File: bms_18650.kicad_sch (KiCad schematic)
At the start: 8 parts, among them IC1 BQ298000RUGR, IC2 EFC8811R-TF

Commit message: updates
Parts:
- added J1: ~, Library:ENFITNIX_BAT, symbol enfitnix_bat_connector:concentric_rings
- C1, C2: footprint (none) -> Capacitor_SMD:C_0805_2012Metric_Pad1.18x1.45mm_HandSolder
- R3, R4, R5: footprint (none) -> Resistor_SMD:R_0805_2012Metric_Pad1.20x1.40mm_HandSolder
- R_SEN1: renamed from R_SEN; footprint (none) -> Resistor_SMD:R_0805_2012Metric_Pad1.20x1.40mm_HandSolder
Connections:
- net GND: now also J1.2 (-)
- net LINK+: now also J1.1 (+)
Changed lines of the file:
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@@
+	)
+	(junction
+		(at 151.13 54.61)
+		(diameter 0)
+		(color 0 0 0 0)
 	)
 	(junction
@@
 	)
 	(junction
+		(at 151.13 124.46)
+		(diameter 0)
+		(color 0 0 0 0)
+	)
+	(junction
 		(at 107.95 124.46)
 		(diameter 0)
@@
 	(wire
 		(pts
-			(xy 140.97 54.61) (xy 157.48 54.61)
+			(xy 140.97 54.61) (xy 151.13 54.61)
 		)
 		(stroke
@@
 	(wire
 		(pts
+			(xy 151.13 67.31) (xy 151.13 54.61)
+		)
+		(stroke
+			(width 0)
+			(type default)
+		)
+	)
+	(wire
+		(pts
 			(xy 55.88 54.61) (xy 55.88 71.12)
 		)
@@
 	(wire
 		(pts
+			(xy 151.13 54.61) (xy 157.48 54.61)
+		)
+		(stroke
+			(width 0)
+			(type default)
+		)
+	)
+	(wire
+		(pts
 			(xy 121.92 54.61) (xy 133.35 54.61)
 		)
@@
 	(wire
 		(pts
-			(xy 107.95 124.46) (xy 153.67 124.46)
+			(xy 107.95 124.46) (xy 151.13 124.46)
+		)
+		(stroke
+			(width 0)
+			(type default)
+		)
+	)
+	(wire
+		(pts
+			(xy 151.13 124.46) (xy 153.67 124.46)
 		)
 		(stroke
@@
 	(wire
 		(pts
+			(xy 151.13 73.66) (xy 151.13 124.46)
+		)
+		(stroke
+			(width 0)
+			(type default)
+		)
+	)
+	(wire
+		(pts
 			(xy 140.97 97.79) (xy 140.97 54.61)
 		)
@@
 	(wire
 		(pts
+			(xy 158.75 67.31) (xy 151.13 67.31)
+		)
+		(stroke
+			(width 0)
+			(type default)
+		)
+	)
+	(wire
+		(pts
 			(xy 55.88 71.12) (xy 55.88 97.79)
 		)
@@
 		(pts
 			(xy 107.95 124.46) (xy 92.71 124.46)
+		)
+		(stroke
+			(width 0)
+			(type default)
+		)
+	)
+	(wire
+		(pts
+			(xy 158.75 73.66) (xy 151.13 73.66)
 		)
 		(stroke
@@
 			)
 		)
-		(property "Footprint" ""
+		(property "Footprint" "Capacitor_SMD:C_0805_2012Metric_Pad1.18x1.45mm_HandSolder"
 			(at 78.4352 97.79 0)
 			(effects
@@
 			)
 		)
-		(property "Footprint" ""
+		(property "Footprint" "Capacitor_SMD:C_0805_2012Metric_Pad1.18x1.45mm_HandSolder"
 			(at 78.4352 78.74 0)
 			(effects
@@
 				(path "/463bbe92-7f47-47ca-96a4-4d541ad2c704"
 					(reference "C1")
+					(unit 1)
+				)
+			)
+		)
+	)
+	(symbol
+		(lib_id "enfitnix_bat_connector:concentric_rings")
+		(at 168.91 67.31 0)
+		(unit 1)
+		(exclude_from_sim no)
+		(in_bom yes)
+		(on_board yes)
+		(dnp no)
+		(fields_autoplaced yes)
+		(property "Reference" "J1"
+			(at 177.8 66.6749 0)
+			(effects
+				(font
+					(size 1.27 1.27)
+				)
+				(justify left)
+			)
+		)
+		(property "Value" "~"
+			(at 177.8 68.58 0)
+			(effects
+				(font
+					(size 1.27 1.27)
+				)
+				(justify left)
+			)
+		)
+		(property "Footprint" "Library:ENFITNIX_BAT"
+			(at 168.91 67.31 0)
+			(effects
+				(font
+					(size 1.27 1.27)
+				)
+				(hide yes)
+			)
+		)
+		(property "Datasheet" ""
+			(at 168.91 67.31 0)
+			(effects
+				(font
+					(size 1.27 1.27)
+				)
+				(hide yes)
+			)
+		)
+		(property "Description" ""
+			(at 168.91 67.31 0)
+			(effects
+				(font
+					(size 1.27 1.27)
+				)
+				(hide yes)
+			)
+		)
+		(pin "1"
+		)
+		(pin "2"
+		)
+		(instances
+			(project ""
+				(path "/463bbe92-7f47-47ca-96a4-4d541ad2c704"
+					(reference "J1")
 					(unit 1)
 				)
@@
 			)
 		)
-		(property "Footprint" ""
+		(property "Footprint" "Resistor_SMD:R_0805_2012Metric_Pad1.20x1.40mm_HandSolder"
 			(at 137.16 96.012 90)
 			(effects
@@
 		(dnp no)
 		(fields_autoplaced yes)
-		(property "Reference" "R_SEN"
+		(property "Reference" "R_SEN1"
 			(at 110.49 116.8399 0)
 			(effects
@@
 			)
 		)
-		(property "Footprint" ""
+		(property "Footprint" "Resistor_SMD:R_0805_2012Metric_Pad1.20x1.40mm_HandSolder"
 			(at 106.172 118.11 90)
 			(effects
@@
 			(project ""
 				(path "/463bbe92-7f47-47ca-96a4-4d541ad2c704"
-					(reference "R_SEN")
+					(reference "R_SEN1")
 					(unit 1)
 				)
@@
 			)
 		)
-		(property "Footprint" ""
+		(property "Footprint" "Resistor_SMD:R_0805_2012Metric_Pad1.20x1.40mm_HandSolder"
 			(at 67.31 96.012 90)
 			(effects
@@
 			)
 		)
-		(property "Footprint" ""
+		(property "Footprint" "Resistor_SMD:R_0805_2012Metric_Pad1.20x1.40mm_HandSolder"
 			(at 67.31 69.342 90)
 			(effects

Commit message: first ordered revision
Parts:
- added J2: ~, Library:CELL_LEAD_CONN, symbol enfitnix_bat_connector:two_conn_leads
- C1, C2: value 0.1uF -> 100n
- IC1: value BQ298000RUGR -> BQ298218RUGR; LCSC (none) -> C36857140
- IC2: LCSC (none) -> C895369
- J1: now not fitted
- R3: value 330 -> 330R
- R4: value 20 -> 20R
- R5: value 2k -> 2K
- R_SEN1: value 0.001 -> 0R001; LCSC (none) -> C4337252
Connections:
- net CELL+: now also J2.1 (CELL+)
- net GND: now also J2.2 (CELL-)
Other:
- note added: "BQ298218 has OCC=-18mV and OCD=40mV so max current with R_SEN1=1mOhm => dchg: 40A => chg: 18A"
- moved on the sheet: C1, C2, IC1, IC2, R3, R4, R5, R_SEN1

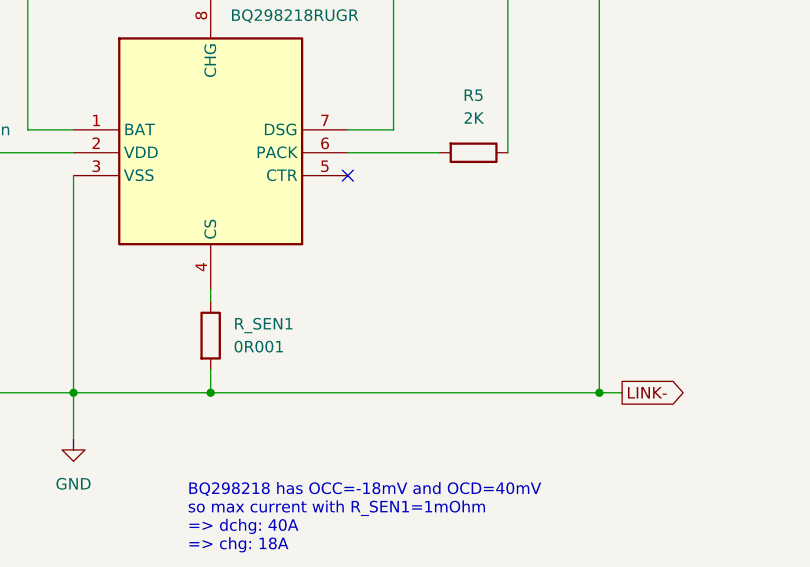
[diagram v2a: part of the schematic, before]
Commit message: fix footprint
fixes issue #1
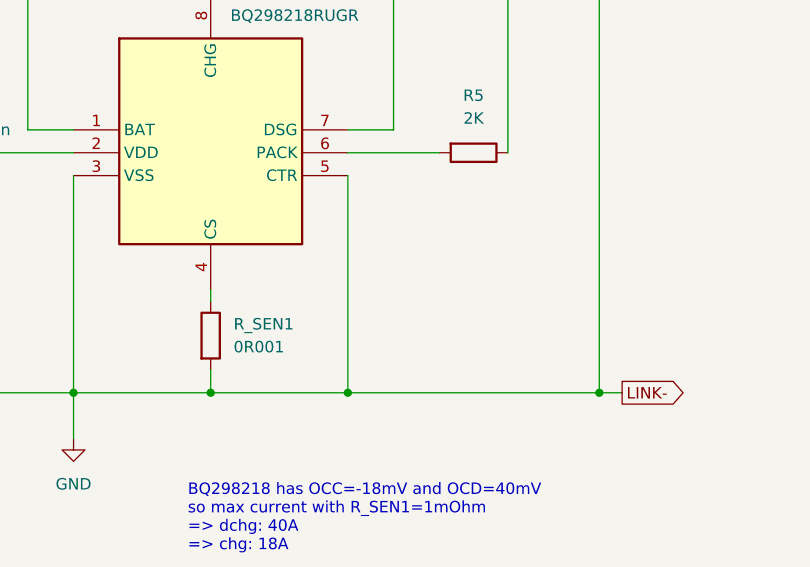
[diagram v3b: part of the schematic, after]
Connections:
- net GND: now also IC1.5 (CTR)
- no-connect marks 1 -> 0
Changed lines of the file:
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@@
 		(color 0 0 0 0)
 	)
-	(no_connect
-		(at 175.26 104.14)
+	(junction
+		(at 175.26 128.27)
+		(diameter 0)
+		(color 0 0 0 0)
 	)
 	(wire
@@
 	(wire
 		(pts
+			(xy 175.26 128.27) (xy 203.2 128.27)
+		)
+		(stroke
+			(width 0)
+			(type default)
+		)
+	)
+	(wire
+		(pts
 			(xy 87.63 83.82) (xy 87.63 128.27)
 		)
@@
 		(pts
 			(xy 185.42 58.42) (xy 185.42 63.5)
+		)
+		(stroke
+			(width 0)
+			(type default)
+		)
+	)
+	(wire
+		(pts
+			(xy 175.26 104.14) (xy 175.26 128.27)
 		)
 		(stroke
@@
 	(wire
 		(pts
-			(xy 160.02 128.27) (xy 203.2 128.27)
+			(xy 160.02 128.27) (xy 175.26 128.27)
 		)
 		(stroke
